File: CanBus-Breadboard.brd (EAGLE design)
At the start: 58.4 x 15.9 mm, 3 parts

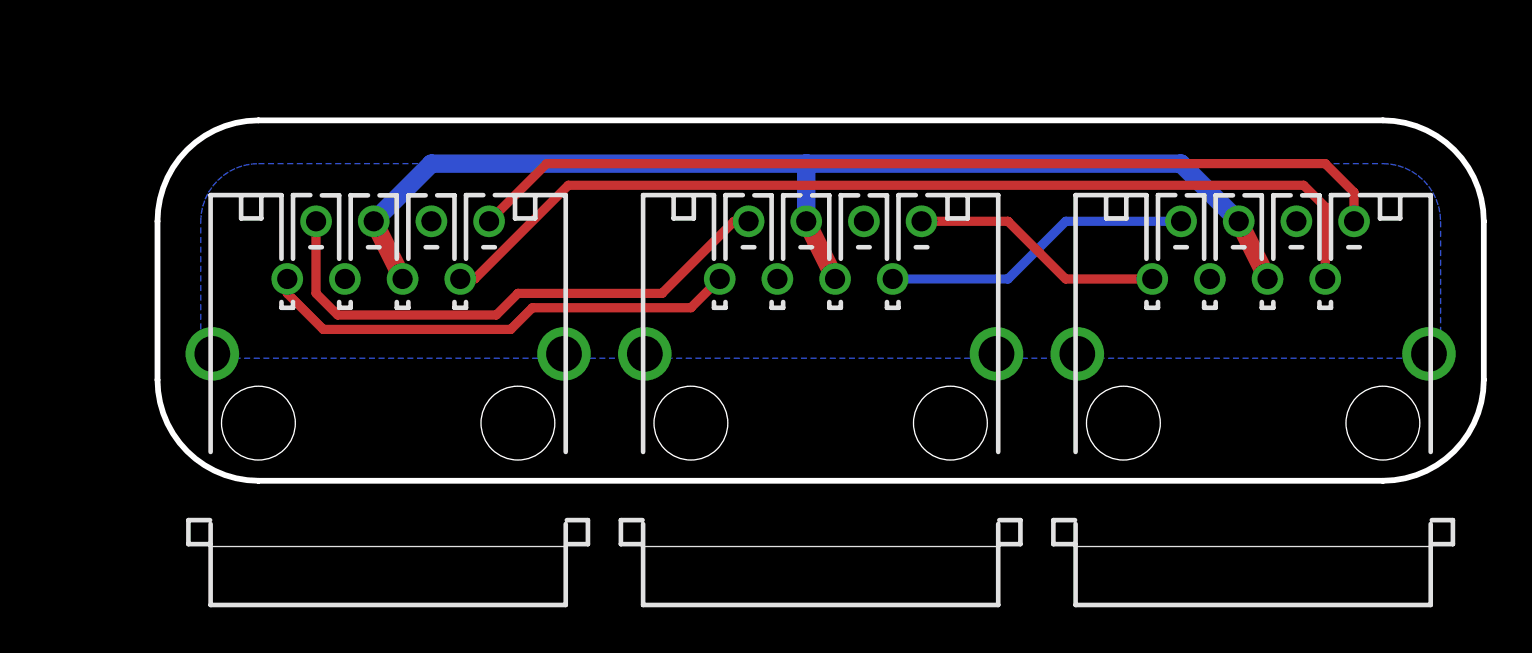
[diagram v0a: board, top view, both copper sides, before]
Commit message: CAN-Bus Beadboard-Adapter, Layouts angepasst
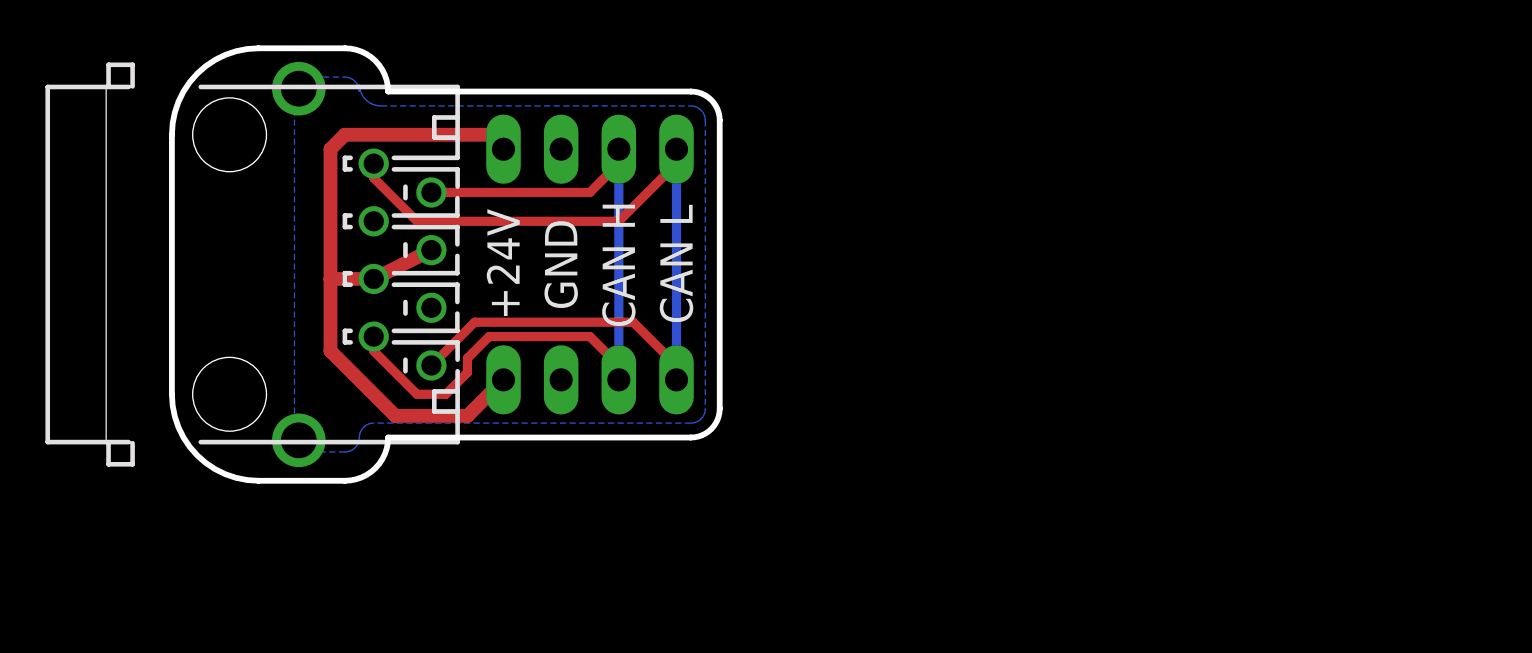
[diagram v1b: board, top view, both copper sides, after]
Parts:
- removed J2, J3: (no value), mebp_8-8g:MEBP_8-8G
- added JP1, JP2: (no value), pinhead:1X04
- moved J1 9.88 mm to (2.54, 9.53), turned to 270 degrees
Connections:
- removed net CANH_1-2: J1.2, J2.2
- removed net CANH_2-3: J2.7, J3.2
- removed net CANH_3-1: J1.7, J3.7
- removed net CANL_1-2: J1.1, J2.1
- removed net CANL_2-3: J2.8, J3.1
- removed net CANL_3-1: J1.8, J3.8
- new net CANH: J1.2, J1.7, JP1.3, JP2.3
- new net CANL: J1.1, J1.8, JP1.4, JP2.4
- net +24V: now also JP1.1, JP2.1; no longer J2.4, J2.5, J3.4, J3.5
- net GND: now also JP1.2, JP2.2; no longer J2.3, J2.6, J2.G1, J2.G2, J3.3, J3.6, J3.G1, J3.G2
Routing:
- net CANH_3-1: track 43.4 -> 0.00 mm
- net CANL_3-1: track 40.9 -> 0.00 mm
- net CANL: track 0.00 -> 39.6 mm
- net CANH: track 0.00 -> 34.4 mm
- net CANH_1-2: track 24.3 -> 0.00 mm
- net CANL_1-2: track 21.3 -> 0.00 mm
- net +24V: track 51.3 -> 31.2 mm
- net CANH_2-3: track 13.8 -> 0.00 mm
- net CANL_2-3: track 11.2 -> 0.00 mm
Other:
- board size 58.4 x 15.9 mm -> 24.1 x 19.1 mm
- board text added: "+24V"
- board text added: "CAN H"
- board text added: "CAN L"
- board text added: "CAN-Bus Beadboard- Adapter"
- board text added: "GND"
- board text removed: "1"
- board text removed: "2"
- board text removed: "3"
- board text removed: "CAN-Bus Y-Verteiler"
